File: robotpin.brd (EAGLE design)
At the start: 30.5 x 39.4 mm, 10 parts

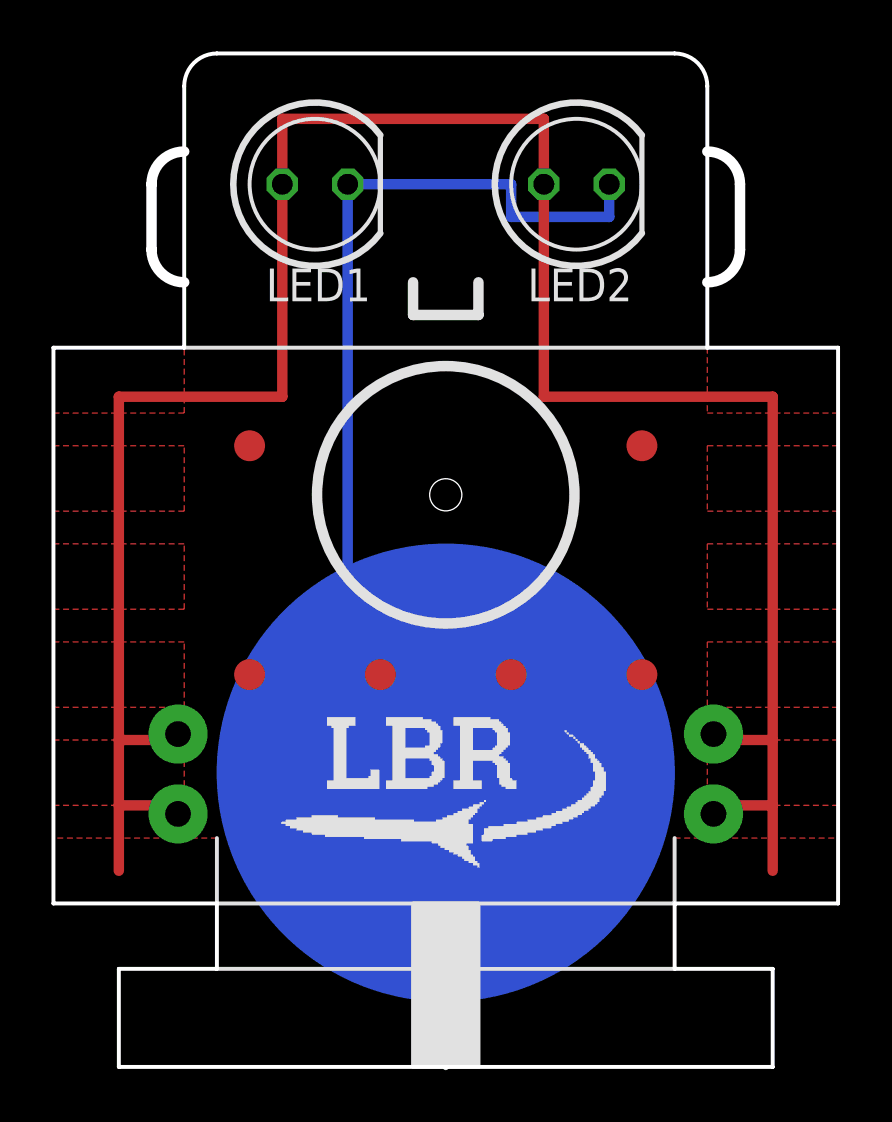
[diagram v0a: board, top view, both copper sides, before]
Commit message: changed unicorn schematic so that all leds are in parallel with each other
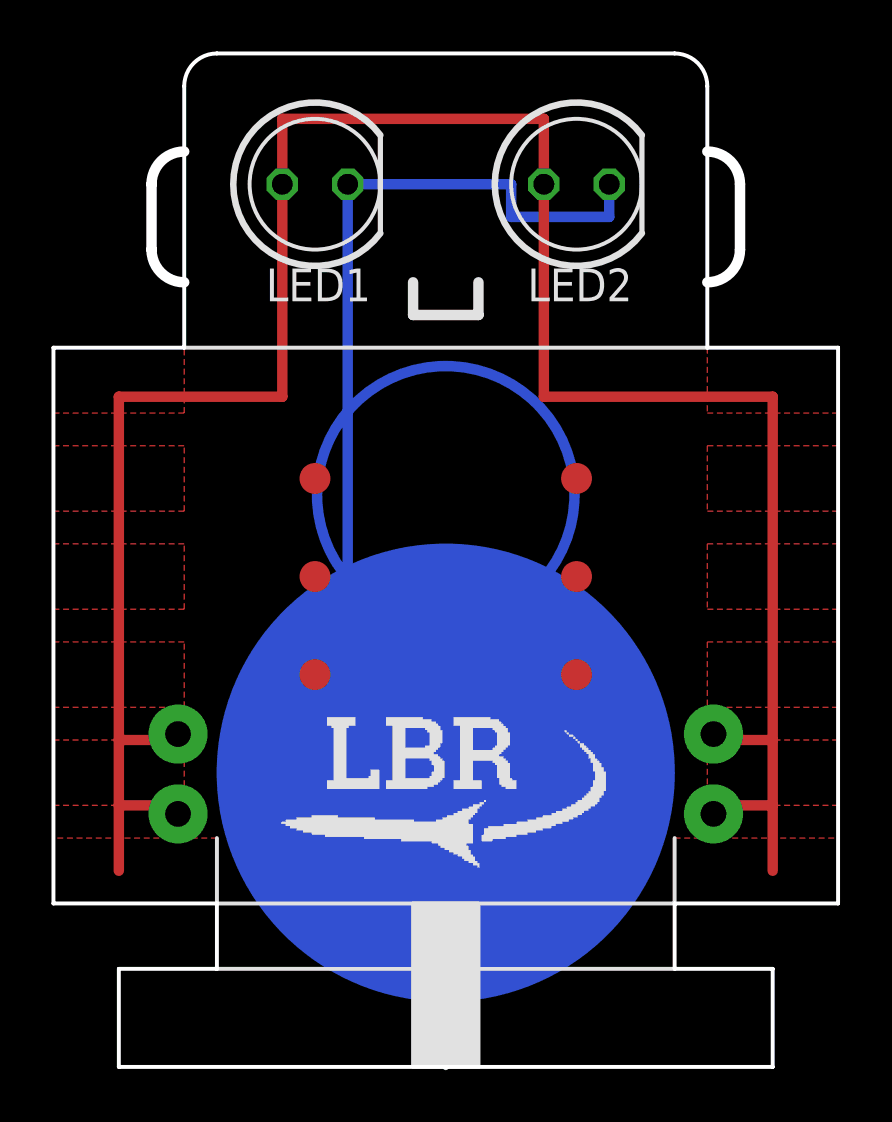
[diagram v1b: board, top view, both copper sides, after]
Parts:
- moved TP1 4.58 mm to (19.1, 27.9)
- moved TP7 4.58 mm to (29.2, 27.9)
- moved TP2 2.84 mm to (19.1, 31.8)
- moved TP8 2.84 mm to (29.2, 31.8)
- moved TP3 2.54 mm to (19.1, 24.1)
- moved TP9 2.54 mm to (29.2, 24.1)
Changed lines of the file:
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@@
 <wire x1="22.86" y1="38.1" x2="25.4" y2="38.1" width="0.4064" layer="25"/>
 <wire x1="25.4" y1="38.1" x2="25.4" y2="39.37" width="0.4064" layer="25"/>
-<hole x="24.13" y="31.115" drill="1.25"/>
-<circle x="24.13" y="31.115" radius="5" width="0.4064" layer="25"/>
+<circle x="24.13" y="31.115" radius="5" width="0.4064" layer="16"/>
 <wire x1="24.13" y1="8.89" x2="24.13" y2="12.7" width="0.254" layer="25"/>
 <wire x1="13.97" y1="36.83" x2="13.97" y2="39.37" width="0.1524" layer="20"/>
@@
 <element name="BATTERY" library="battery" package="BAT-HLD-001-THM" value="CR2032-GK" x="24.13" y="20.32" rot="MR0"/>
 <element name="U$2" library="LBR Logo" package="LOGO-0.50&quot;" value="" x="17.78" y="16.51"/>
-<element name="TP1" library="testpad" package="TP12R" value="PTR1TP12R" x="16.51" y="24.13" smashed="yes">
-<attribute name="TP_SIGNAL_NAME" value="" x="16.51" y="21.59" size="1" layer="37"/>
-<attribute name="VALUE" x="16.002" y="23.495" size="0.0254" layer="27"/>
-</element>
-<element name="TP2" library="testpad" package="TP12R" value="PTR1TP12R" x="16.51" y="33.02" smashed="yes">
-<attribute name="TP_SIGNAL_NAME" value="" x="16.51" y="30.48" size="1" layer="37"/>
-<attribute name="VALUE" x="16.002" y="32.385" size="0.0254" layer="27"/>
-</element>
-<element name="TP3" library="testpad" package="TP12R" value="PTR1TP12R" x="21.59" y="24.13" smashed="yes">
-<attribute name="TP_SIGNAL_NAME" value="" x="21.59" y="21.59" size="1" layer="37"/>
-<attribute name="VALUE" x="21.082" y="23.495" size="0.0254" layer="27"/>
-</element>
-<element name="TP7" library="testpad" package="TP12R" value="PTR1TP12R" x="31.75" y="24.13" smashed="yes">
-<attribute name="TP_SIGNAL_NAME" value="" x="31.75" y="21.59" size="1" layer="37"/>
-<attribute name="VALUE" x="31.242" y="23.495" size="0.0254" layer="27"/>
-</element>
-<element name="TP8" library="testpad" package="TP12R" value="PTR1TP12R" x="31.75" y="33.02" smashed="yes">
-<attribute name="TP_SIGNAL_NAME" value="" x="31.75" y="30.48" size="1" layer="37"/>
-<attribute name="VALUE" x="31.242" y="32.385" size="0.0254" layer="27"/>
-</element>
-<element name="TP9" library="testpad" package="TP12R" value="PTR1TP12R" x="26.67" y="24.13" smashed="yes">
-<attribute name="TP_SIGNAL_NAME" value="" x="26.67" y="21.59" size="1" layer="37"/>
-<attribute name="VALUE" x="26.162" y="23.495" size="0.0254" layer="27"/>
+<element name="TP1" library="testpad" package="TP12R" value="PTR1TP12R" x="19.05" y="27.94" smashed="yes">
+<attribute name="TP_SIGNAL_NAME" value="" x="19.05" y="25.4" size="1" layer="37"/>
+<attribute name="VALUE" x="18.542" y="27.305" size="0.0254" layer="27"/>
+</element>
+<element name="TP2" library="testpad" package="TP12R" value="PTR1TP12R" x="19.05" y="31.75" smashed="yes">
+<attribute name="TP_SIGNAL_NAME" value="" x="19.05" y="29.21" size="1" layer="37"/>
+<attribute name="VALUE" x="18.542" y="31.115" size="0.0254" layer="27"/>
+</element>
+<element name="TP3" library="testpad" package="TP12R" value="PTR1TP12R" x="19.05" y="24.13" smashed="yes">
+<attribute name="TP_SIGNAL_NAME" value="" x="19.05" y="21.59" size="1" layer="37"/>
+<attribute name="VALUE" x="18.542" y="23.495" size="0.0254" layer="27"/>
+</element>
+<element name="TP7" library="testpad" package="TP12R" value="PTR1TP12R" x="29.21" y="27.94" smashed="yes">
+<attribute name="TP_SIGNAL_NAME" value="" x="29.21" y="25.4" size="1" layer="37"/>
+<attribute name="VALUE" x="28.702" y="27.305" size="0.0254" layer="27"/>
+</element>
+<element name="TP8" library="testpad" package="TP12R" value="PTR1TP12R" x="29.21" y="31.75" smashed="yes">
+<attribute name="TP_SIGNAL_NAME" value="" x="29.21" y="29.21" size="1" layer="37"/>
+<attribute name="VALUE" x="28.702" y="31.115" size="0.0254" layer="27"/>
+</element>
+<element name="TP9" library="testpad" package="TP12R" value="PTR1TP12R" x="29.21" y="24.13" smashed="yes">
+<attribute name="TP_SIGNAL_NAME" value="" x="29.21" y="21.59" size="1" layer="37"/>
+<attribute name="VALUE" x="28.702" y="23.495" size="0.0254" layer="27"/>
 </element>
 </elements>
